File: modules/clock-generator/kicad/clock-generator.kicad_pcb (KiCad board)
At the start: 2 copper layers, 22 parts, among them IC1 ATTINY84-S, P1 CONN_01X03, P2 CONN_02X03, P3 CONN_01X09, Q1 Q_NPN_BEC, SW1 SW_PUSH, SW2 SW_PUSH, U1 MAX7221, U2 4024, Y1 16MHz

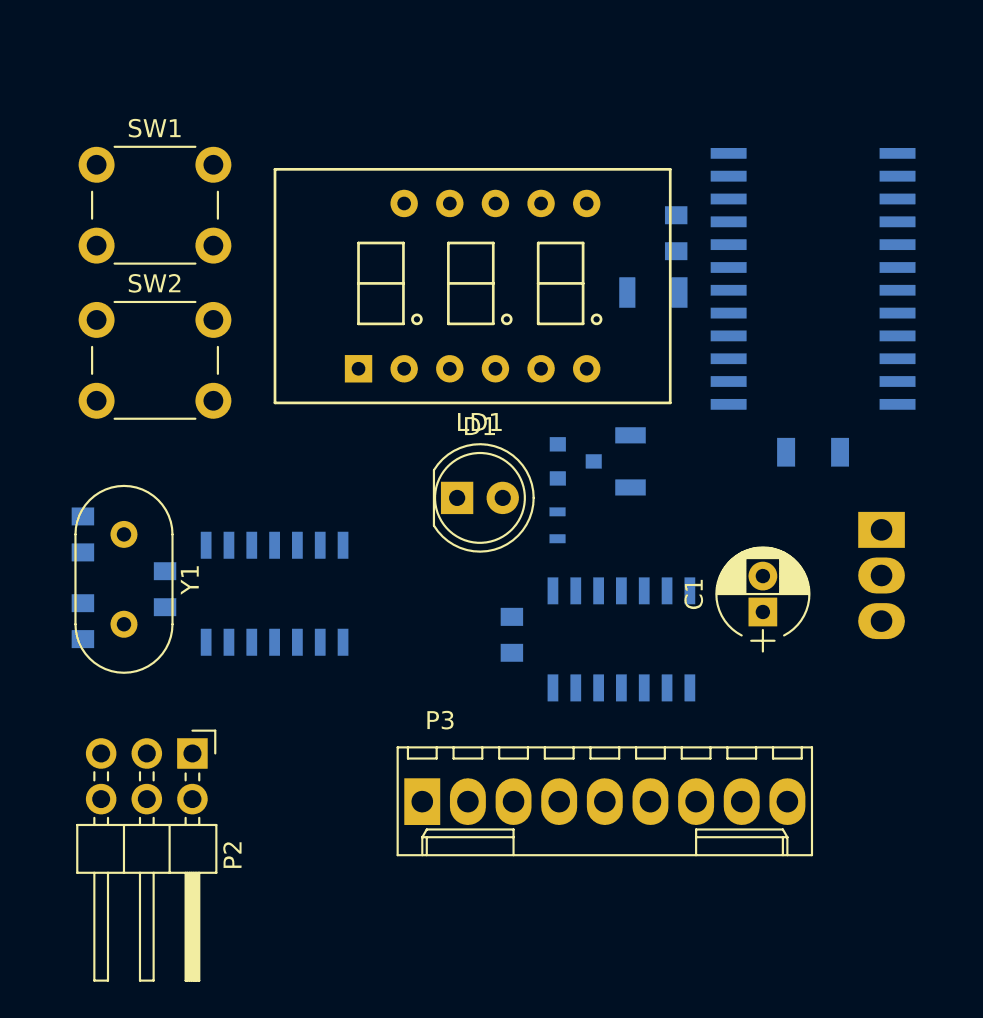
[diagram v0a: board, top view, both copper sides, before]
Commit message: Clock gen pcb: routed all but the power nets
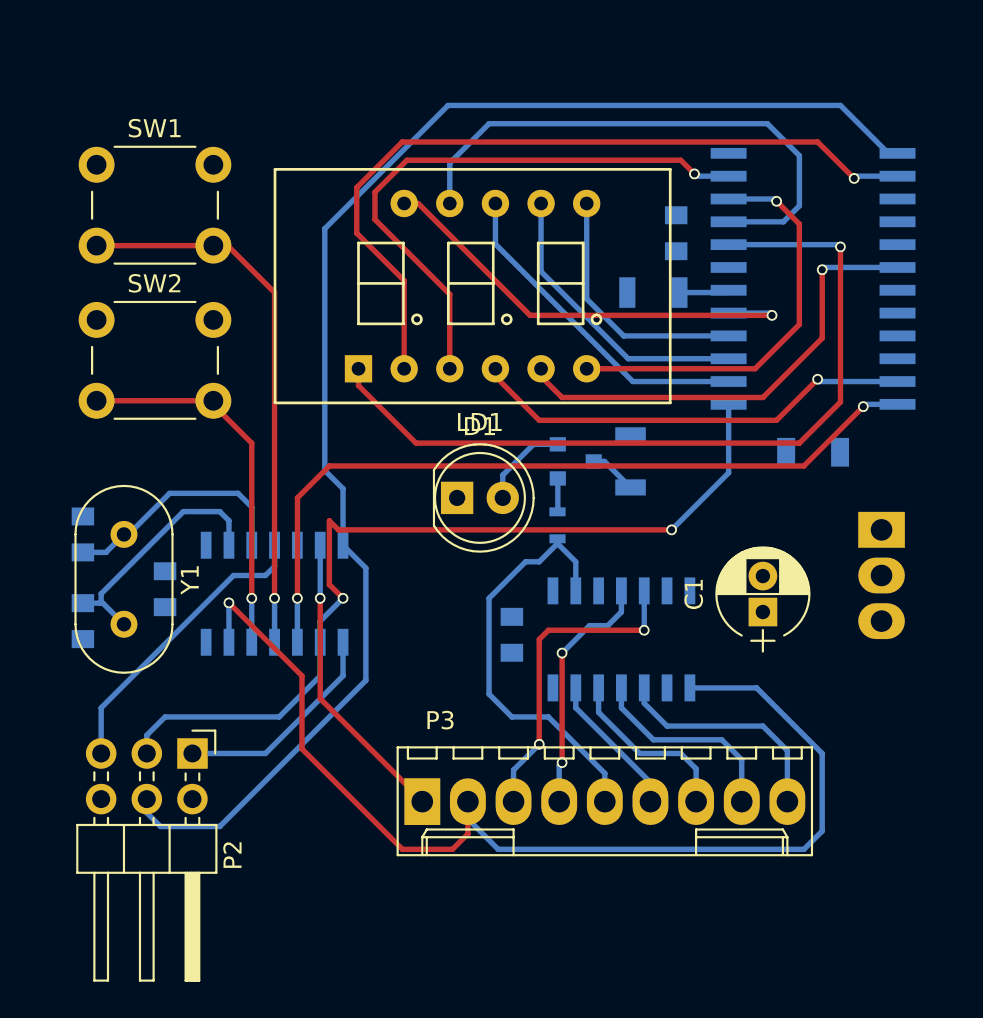
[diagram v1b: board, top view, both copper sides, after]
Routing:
- net Net-(IC1-Pad7): track 0.00 -> 78.6 mm
- net THIRTYSECOND_OUT: track 0.00 -> 60.7 mm, vias 0 -> 1
- net Net-(IC1-Pad9): track 0.00 -> 49.1 mm, vias 0 -> 2
- net Net-(LD1-Pad1): track 0.00 -> 44.9 mm, vias 0 -> 1
- net Net-(IC1-Pad10): track 0.00 -> 43.6 mm, vias 0 -> 2
- net Net-(LD1-Pad2): track 0.00 -> 43.2 mm, vias 0 -> 1
- net Net-(LD1-Pad3): track 0.00 -> 32.3 mm, vias 0 -> 1
- net Net-(LD1-Pad10): track 0.00 -> 30.5 mm
- net Net-(IC1-Pad11): track 0.00 -> 30.5 mm, vias 0 -> 1
- net Net-(LD1-Pad5): track 0.00 -> 26.0 mm, vias 0 -> 1
- net Net-(LD1-Pad11): track 0.00 -> 25.5 mm, vias 0 -> 1
- net Net-(LD1-Pad4): track 0.00 -> 24.8 mm, vias 0 -> 1
- net QUARTER_OUT: track 0.00 -> 23.6 mm
- net Net-(LD1-Pad6): track 0.00 -> 23.0 mm, vias 0 -> 1
- net Net-(IC1-Pad12): track 0.00 -> 20.8 mm, vias 0 -> 1
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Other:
- net class Default: clearance 0.2 -> 0.3; trace_width 0.25 -> 0.3
- rule trace_clearance: 0.2 -> 0.3

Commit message: Finish clock generator PCB, start panel
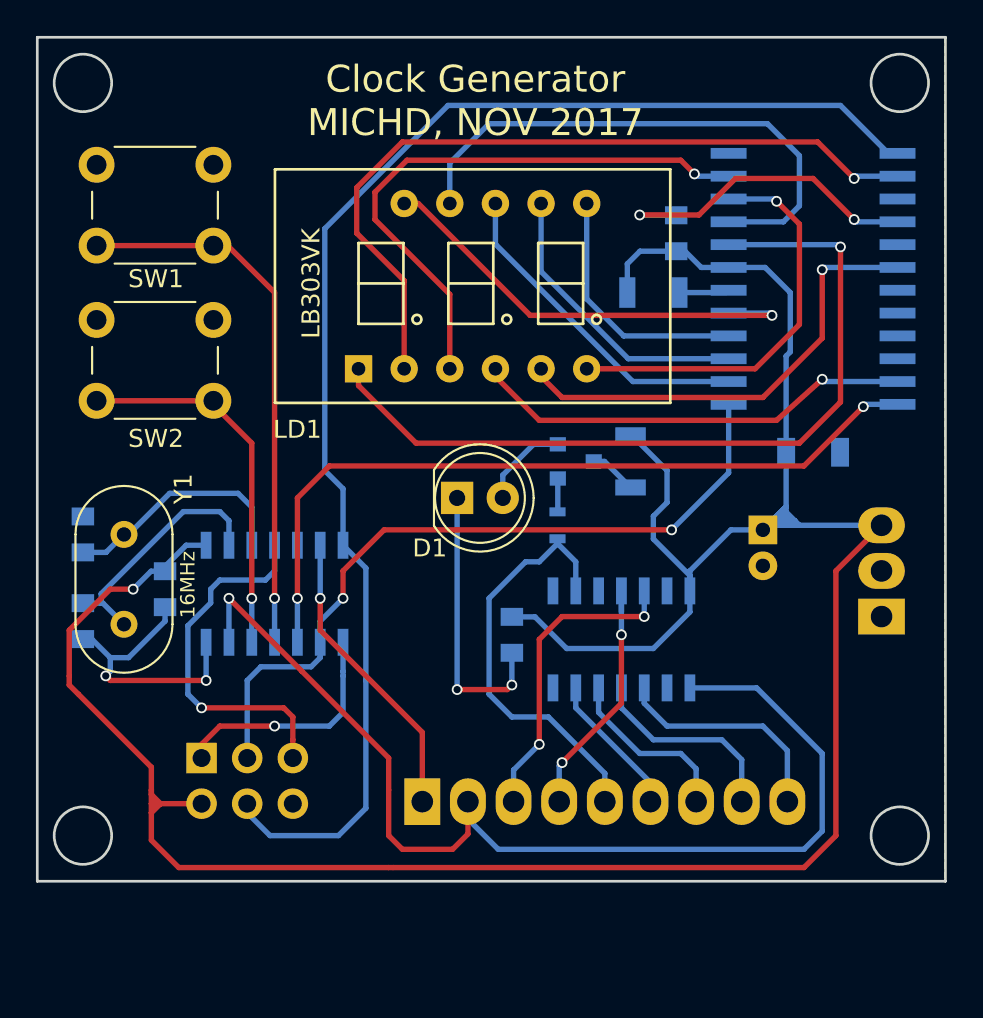
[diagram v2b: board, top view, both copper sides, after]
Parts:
- C1, P3: moved to B.Cu
- IC1: value ATTINY84-S -> ATTINY84
- LD1: value LB303AK -> LB303VK
- P2: footprint Pin_Headers:Pin_Header_Angled_2x03_Pitch2.54mm -> Pin_Headers:Pin_Header_Straight_2x03_Pitch2.54mm; moved to B.Cu
- moved P1 4.83 mm to (182.6, 100.3), turned to 90 degrees
- moved C1 4.57 mm to (176.0, 95.5), turned to 270 degrees
- moved P2 0.57 mm to (144.8, 108.2)
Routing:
- net VCC: track 0.00 -> 156.7 mm, vias 0 -> 1
- net GND: track 0.00 -> 49.4 mm, vias 0 -> 6
- net Net-(IC1-Pad9): track 49.1 -> 41.8 mm
- net Net-(IC1-Pad4): track 16.6 -> 20.4 mm, vias 0 -> 1
- net Net-(IC1-Pad8): track 12.0 -> 13.3 mm, vias 0 -> 1
- net Net-(IC1-Pad7): track 78.6 -> 77.8 mm
- net EIGHTH_OUT: track 13.8 -> 14.3 mm
- net THIRTYSECOND_OUT: track 60.7 -> 61.2 mm
- added copper zone on B.Cu, net GND
- added copper zone on F.Cu, net GND
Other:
- board outline added: 50.5 x 47 mm
- board text added: "Clock Generator MICHD, NOV 2017"
- board text added: "ISP"
- board text added: "VCC"
